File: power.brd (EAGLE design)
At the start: 65 x 80 mm, 21 parts, among them J1 Battery, J2 Solar, J3 Valve, J4 Button

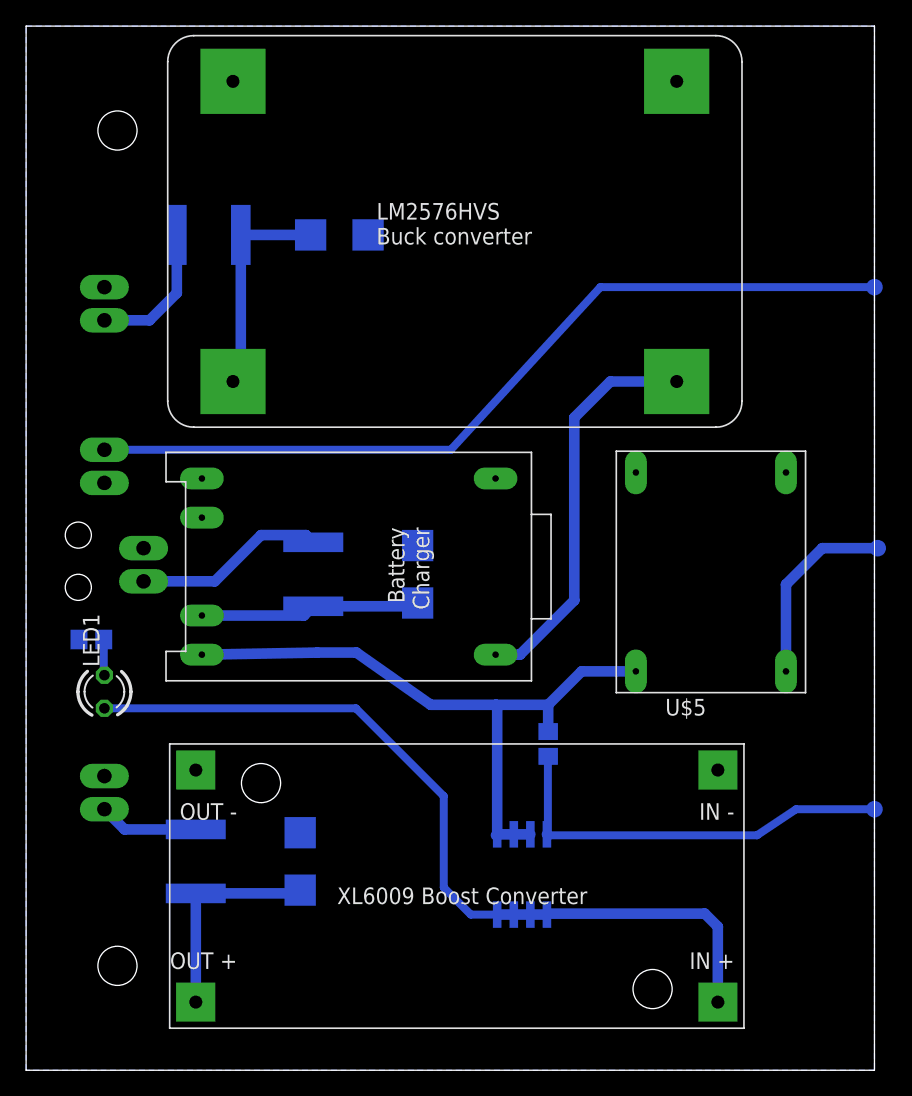
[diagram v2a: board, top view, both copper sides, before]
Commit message: Replaced PTC
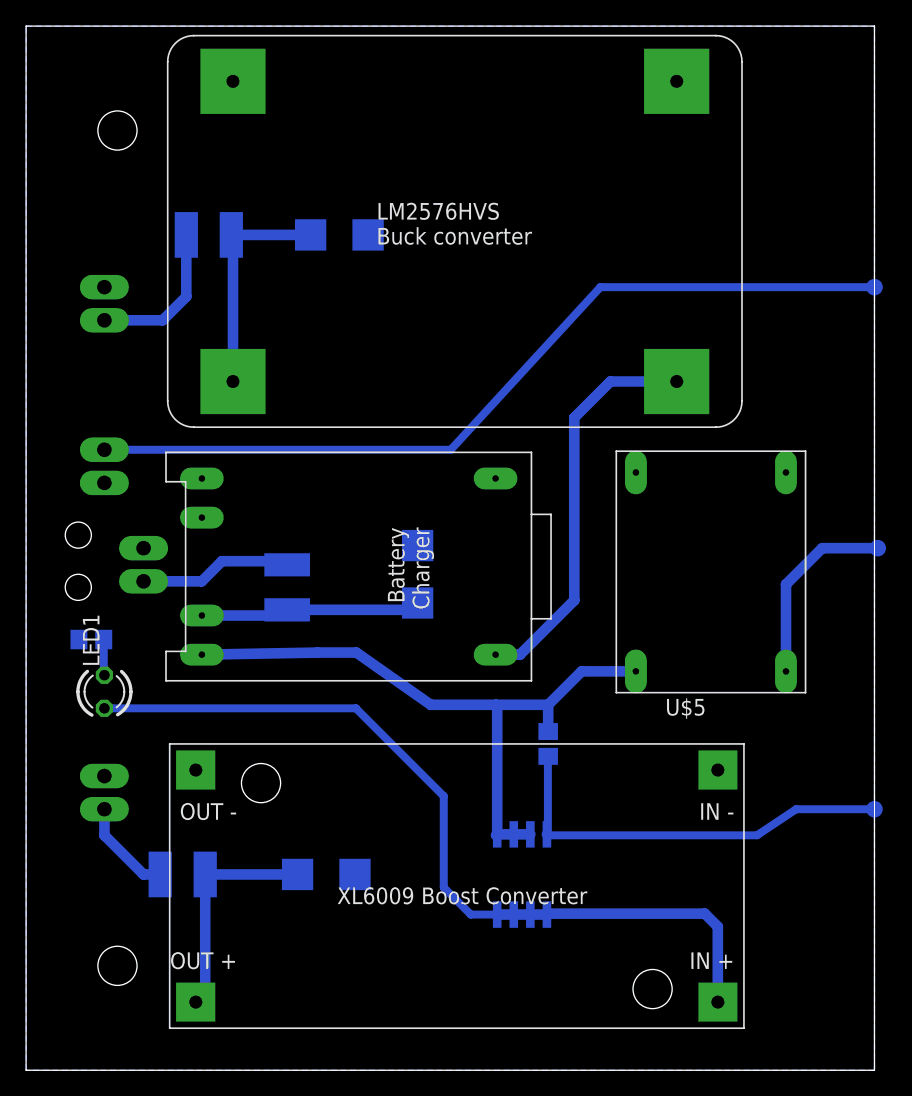
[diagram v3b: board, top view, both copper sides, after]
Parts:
- removed U$10: 500mA, fuse:MF-SMDF050
- removed U$11: 2A, fuse:MF-SMDF050
- added U$1: 1A, Semiconductors:1812
- added U$4: 2A, Semiconductors:1812
- D2, D3, D4: value (none) -> SJ24
- U$3: value 1A -> 2A; device fuse:MF-SMDF050 -> Semiconductors:1812
- moved D4 2.24 mm to (23.0, 15.0), turned to 180 degrees
- moved U$3 1.41 mm to (12.0, 15.0)
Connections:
- net N$3: now also U$4.P$1; no longer U$11.1
- net N$36: now also U$4.P$2; no longer U$11.2
- net N$6: now also U$3.P$1; no longer U$3.1
- net VALVE: now also U$3.P$2; no longer U$3.2
- net V_SOLAR: now also U$1.P$1; no longer U$10.1
- net V_SOLAR_FUSED: now also U$1.P$2; no longer U$10.2
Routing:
- net N$3: track 14.7 -> 11.8 mm
- net V_SOLAR: track 10.9 -> 11.8 mm
- net N$6: track 16.4 -> 17.2 mm
- net V_SOLAR_FUSED: track 16.8 -> 17.4 mm
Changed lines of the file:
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@@
 <layer number="230" name="230bmp" color="7" fill="1" visible="yes" active="yes"/>
 <layer number="231" name="231bmp" color="7" fill="1" visible="yes" active="yes"/>
+<layer number="232" name="Eagle3D_PG2" color="7" fill="1" visible="yes" active="yes"/>
+<layer number="233" name="Eagle3D_PG3" color="7" fill="1" visible="yes" active="yes"/>
 <layer number="248" name="Housing" color="7" fill="1" visible="yes" active="yes"/>
 <layer number="249" name="Edge" color="7" fill="1" visible="yes" active="yes"/>
@@
 </autorouter>
 <elements>
-<element name="D2" library="diode" library_urn="urn:adsk.eagle:library:210" package="SMB" package3d_urn="urn:adsk.eagle:package:43404/2" value="" x="24" y="64" rot="MR180"/>
-<element name="D3" library="diode" library_urn="urn:adsk.eagle:library:210" package="SMB" package3d_urn="urn:adsk.eagle:package:43404/2" value="" x="30" y="38" rot="MR90"/>
+<element name="D2" library="diode" library_urn="urn:adsk.eagle:library:210" package="SMB" package3d_urn="urn:adsk.eagle:package:43404/2" value="SJ24" x="24" y="64" rot="MR180"/>
+<element name="D3" library="diode" library_urn="urn:adsk.eagle:library:210" package="SMB" package3d_urn="urn:adsk.eagle:package:43404/2" value="SJ24" x="30" y="38" rot="MR90"/>
 <element name="J1" library="SparkFun-Connectors" package="1X02_LONGPADS" value="Battery" x="9" y="40" rot="R270"/>
 <element name="J2" library="SparkFun-Connectors" package="1X02_LONGPADS" value="Solar" x="6" y="60" rot="R270"/>
@@
 <attribute name="TP_SIGNAL_NAME" value="" x="65.25" y="40" size="1.778" layer="28" rot="MR0" display="off"/>
 </element>
-<element name="U$10" library="fuse" library_urn="urn:adsk.eagle:library:233" package="MF-SMDF050" package3d_urn="urn:adsk.eagle:package:14081/1" value="500mA" x="14" y="64" rot="MR180"/>
-<element name="U$11" library="fuse" library_urn="urn:adsk.eagle:library:233" package="MF-SMDF050" package3d_urn="urn:adsk.eagle:package:14081/1" value="2A" x="22" y="38" rot="MR270"/>
 <element name="U$2" library="breakout-modules" package="BATTERY_CHARGER" value="BATTERY_CHARGER" x="24.72" y="38.59" rot="R270"/>
 <element name="U$5" library="breakout-modules" package="QSKJ_BOOST_MODULE" value="QSKJ_BOOST_MODULE" x="52.47" y="38.18"/>
@@
 <element name="U$6" library="breakout-modules" package="XL6009_BOOST_MODULE" value="XL6009_BOOST_MODULE" x="53" y="23" rot="R180"/>
 <element name="U$9" library="Semiconductors" package="SO08" value="FDS6675" x="38" y="15" rot="MR180"/>
-<element name="U$3" library="fuse" library_urn="urn:adsk.eagle:library:233" package="MF-SMDF050" package3d_urn="urn:adsk.eagle:package:14081/1" value="1A" x="13" y="16" rot="MR90"/>
-<element name="D4" library="diode" library_urn="urn:adsk.eagle:library:210" package="SMB" package3d_urn="urn:adsk.eagle:package:43404/2" value="" x="21" y="16" rot="MR90"/>
+<element name="D4" library="diode" library_urn="urn:adsk.eagle:library:210" package="SMB" package3d_urn="urn:adsk.eagle:package:43404/2" value="SJ24" x="23" y="15" rot="MR180"/>
 <element name="J3" library="SparkFun-Connectors" package="1X02_LONGPADS" value="Valve" x="6" y="20" rot="R90"/>
 <element name="TP5" library="testpad" library_urn="urn:adsk.eagle:library:385" package="B1,27" package3d_urn="urn:adsk.eagle:package:27944/1" value="TPSB1,27" x="65" y="20" rot="MR0">
@@
 <attribute name="TP_SIGNAL_NAME" value="" x="65" y="60" size="1.778" layer="28" rot="MR90" display="off"/>
 </element>
+<element name="U$1" library="Semiconductors" package="1812" value="1A" x="14" y="64" rot="MR270"/>
+<element name="U$4" library="Semiconductors" package="1812" value="2A" x="20" y="37" rot="MR0"/>
+<element name="U$3" library="Semiconductors" package="1812" value="2A" x="12" y="15" rot="MR90"/>
 </elements>
 <signals>
@@
 <signal name="V_SOLAR_FUSED">
 <contactref element="U$8" pad="IN"/>
-<contactref element="U$10" pad="2"/>
 <contactref element="D2" pad="C"/>
-<wire x1="16.45" y1="64" x2="16.45" y2="53.37" width="0.8128" layer="16"/>
-<wire x1="16.45" y1="53.37" x2="15.85" y2="52.77" width="0.8128" layer="16"/>
-<wire x1="16.45" y1="64" x2="21.8" y2="64" width="0.8128" layer="16"/>
+<contactref element="U$1" pad="P$2"/>
+<wire x1="15.85" y1="52.77" x2="15.85" y2="63.875" width="0.8128" layer="16"/>
+<wire x1="15.85" y1="63.875" x2="15.725" y2="64" width="0.8128" layer="16"/>
+<wire x1="15.725" y1="64" x2="21.8" y2="64" width="0.8128" layer="16"/>
 </signal>
 <signal name="V_UNREG">
@@
 <signal name="V_SOLAR">
 <contactref element="J2" pad="2"/>
-<contactref element="U$10" pad="1"/>
-<wire x1="6" y1="57.46" x2="9.46" y2="57.46" width="0.8128" layer="16"/>
-<wire x1="11.55" y1="59.55" x2="11.55" y2="64" width="0.8128" layer="16"/>
-<wire x1="9.46" y1="57.46" x2="11.55" y2="59.55" width="0.8128" layer="16"/>
+<contactref element="U$1" pad="P$1"/>
+<wire x1="6" y1="57.46" x2="10.46" y2="57.46" width="0.8128" layer="16"/>
+<wire x1="12.275" y1="59.275" x2="12.275" y2="64" width="0.8128" layer="16"/>
+<wire x1="10.46" y1="57.46" x2="12.275" y2="59.275" width="0.8128" layer="16"/>
 </signal>
 <signal name="N$36">
 <contactref element="U$2" pad="V_BATT+"/>
-<contactref element="U$11" pad="2"/>
 <contactref element="D3" pad="C"/>
-<wire x1="13.47" y1="34.84" x2="21.29" y2="34.84" width="0.8128" layer="16"/>
-<wire x1="21.29" y1="34.84" x2="22" y2="35.55" width="0.8128" layer="16"/>
-<wire x1="22" y1="35.55" x2="29.75" y2="35.55" width="0.8128" layer="16"/>
-<wire x1="29.75" y1="35.55" x2="30" y2="35.8" width="0.8128" layer="16"/>
+<contactref element="U$4" pad="P$2"/>
+<wire x1="13.47" y1="34.84" x2="19.565" y2="34.84" width="0.8128" layer="16"/>
+<wire x1="19.565" y1="34.84" x2="20" y2="35.275" width="0.8128" layer="16"/>
+<wire x1="20" y1="35.275" x2="29.475" y2="35.275" width="0.8128" layer="16"/>
+<wire x1="29.475" y1="35.275" x2="30" y2="35.8" width="0.8128" layer="16"/>
 </signal>
 <signal name="N$3">
-<contactref element="U$11" pad="1"/>
 <contactref element="J1" pad="2"/>
-<wire x1="9" y1="37.46" x2="14.46" y2="37.46" width="0.8128" layer="16"/>
-<wire x1="14.46" y1="37.46" x2="18" y2="41" width="0.8128" layer="16"/>
-<wire x1="18" y1="41" x2="21.45" y2="41" width="0.8128" layer="16"/>
-<wire x1="21.45" y1="41" x2="22" y2="40.45" width="0.8128" layer="16"/>
+<contactref element="U$4" pad="P$1"/>
+<wire x1="9" y1="37.46" x2="13.46" y2="37.46" width="0.8128" layer="16"/>
+<wire x1="13.46" y1="37.46" x2="15" y2="39" width="0.8128" layer="16"/>
+<wire x1="15" y1="39" x2="19.725" y2="39" width="0.8128" layer="16"/>
+<wire x1="19.725" y1="39" x2="20" y2="38.725" width="0.8128" layer="16"/>
 </signal>
 <signal name="N$9">
@@
 </signal>
 <signal name="VALVE">
-<contactref element="U$3" pad="2"/>
 <contactref element="J3" pad="1"/>
-<wire x1="6" y1="20" x2="7.55" y2="18.45" width="0.8128" layer="16"/>
-<wire x1="7.55" y1="18.45" x2="13" y2="18.45" width="0.8128" layer="16"/>
+<contactref element="U$3" pad="P$2"/>
+<wire x1="10.275" y1="15" x2="9" y2="15" width="0.8128" layer="16"/>
+<wire x1="9" y1="15" x2="6" y2="18" width="0.8128" layer="16"/>
+<wire x1="6" y1="18" x2="6" y2="20" width="0.8128" layer="16"/>
 </signal>
 <signal name="N$6">
 <contactref element="U$6" pad="V_OUT"/>
-<contactref element="U$3" pad="1"/>
 <contactref element="D4" pad="C"/>
-<wire x1="13" y1="5.22" x2="13" y2="13.55" width="0.8128" layer="16"/>
-<wire x1="13" y1="13.55" x2="20.75" y2="13.55" width="0.8128" layer="16"/>
-<wire x1="20.75" y1="13.55" x2="21" y2="13.8" width="0.8128" layer="16"/>
+<contactref element="U$3" pad="P$1"/>
+<wire x1="13" y1="5.22" x2="13.725" y2="5.945" width="0.8128" layer="16"/>
+<wire x1="13.725" y1="5.945" x2="13.725" y2="15" width="0.8128" layer="16"/>
+<wire x1="13.725" y1="15" x2="20.8" y2="15" width="0.8128" layer="16"/>
 </signal>
 <signal name="BUTTON_WAKEUP_INT">

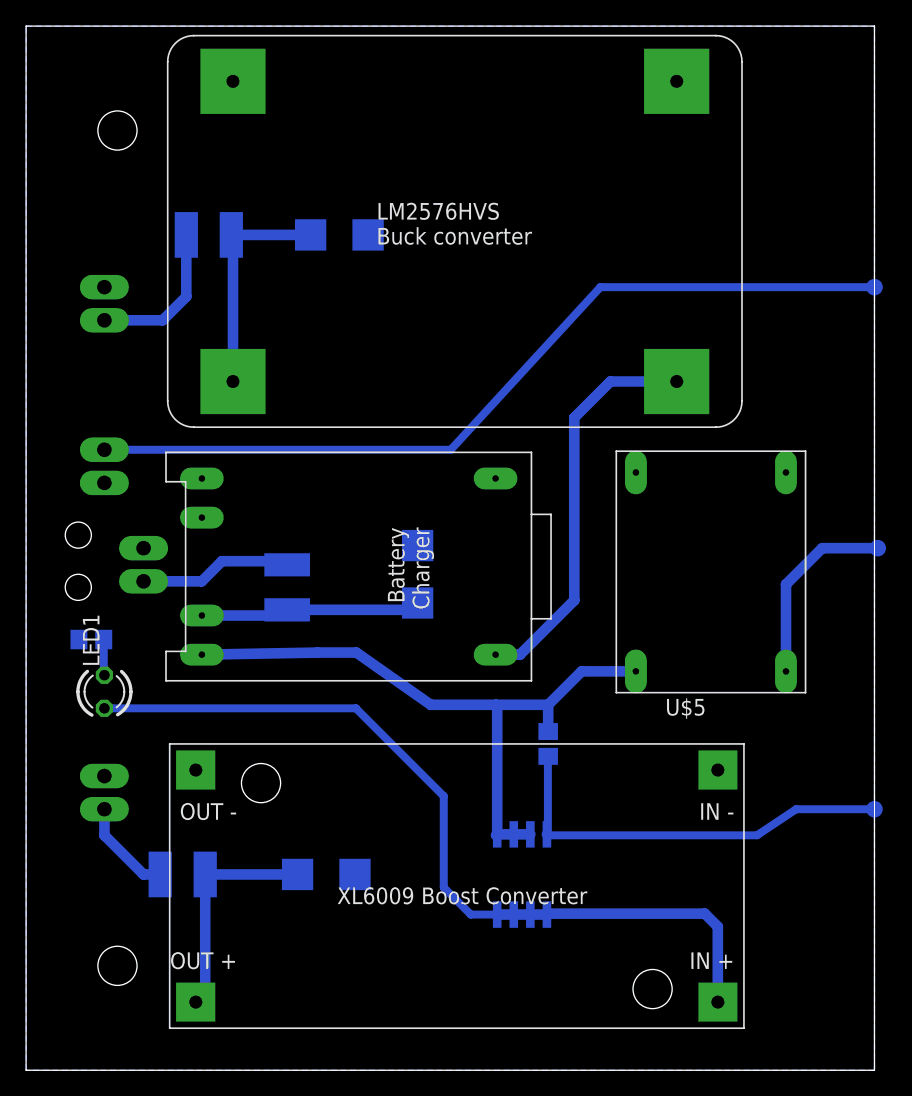
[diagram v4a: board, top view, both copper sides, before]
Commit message: Using CN3791
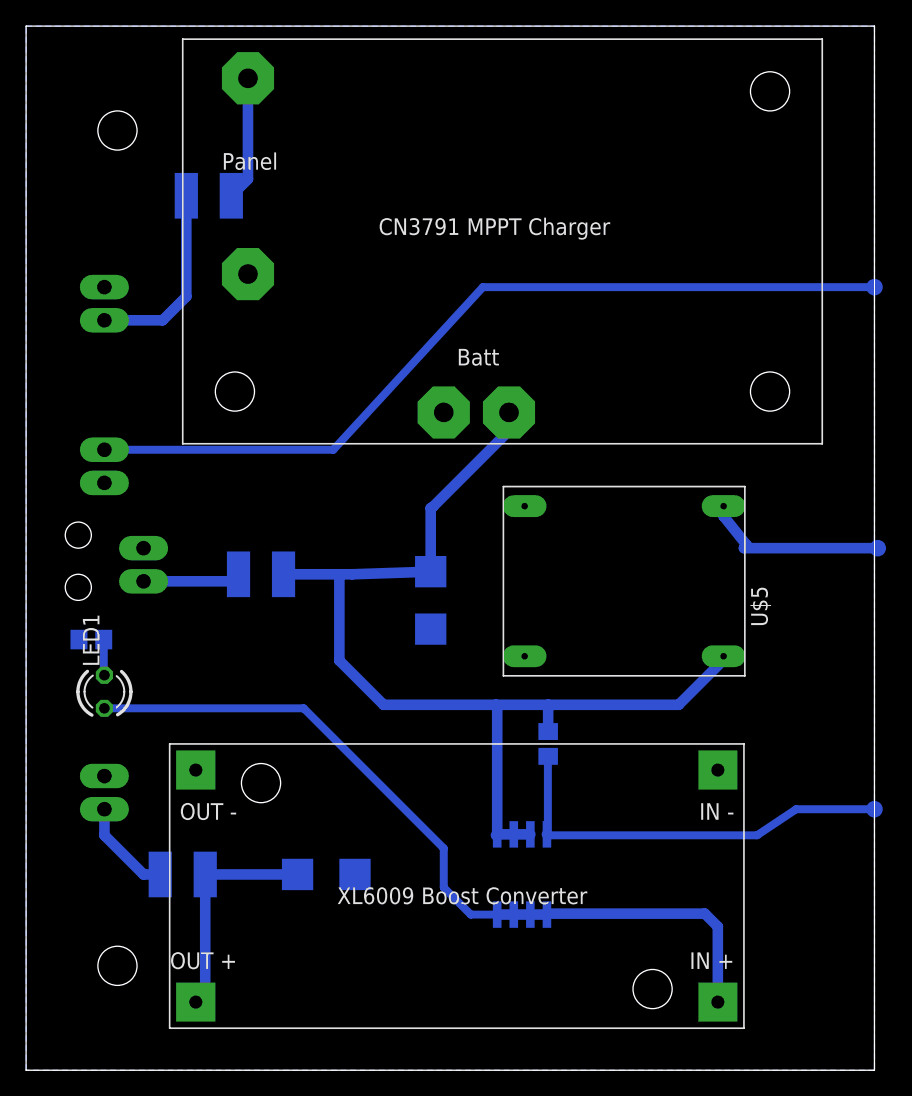
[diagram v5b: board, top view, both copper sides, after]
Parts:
- removed D2: SJ24, diode:SMB
- removed U$8: LM2576HVS_BUCK_MODULE, breakout-modules:LM2576HVS_BUCK_MODULE
- U$2: value BATTERY_CHARGER -> CN3791_MTTP_LIPO_SOLAR_CHARGER; device breakout-modules:BATTERY_CHARGER -> breakout-modules:CN3791_MPPT_LIPO_SOLAR_CHARGER
- moved U$2 15.8 mm to (12.0, 48.0), turned to 0 degrees
- moved U$5 6.69 mm to (45.8, 37.5), turned to 90 degrees
- moved U$1 3.00 mm to (14.0, 67.0)
- moved D3 2.24 mm to (31.0, 36.0), turned to 270 degrees
- moved U$4 2.24 mm to (18.0, 38.0), turned to 270 degrees
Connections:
- removed net N$36: D3.C, U$2.V_BATT+, U$4.P$2
- removed net V_CHARGER: U$2.V_IN, U$8.OUT
- net GND: no longer D2.A, U$2.V_BATT-, U$8.GND@1, U$8.GND@2
- net V_SOLAR_FUSED: now also U$2.PANEL; no longer D2.C, U$8.IN
- net V_UNREG: now also D3.C, U$2.BATT+, U$4.P$2; no longer U$2.V_OUT
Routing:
- net V_CHARGER: track 30.8 -> 0.00 mm
- net V_UNREG: track 50.3 -> 79.8 mm
- net N$36: track 16.9 -> 0.00 mm
- net V_SOLAR_FUSED: track 17.4 -> 9.70 mm
- net N$3: track 11.8 -> 7.50 mm
- net V_SOLAR: track 11.8 -> 14.8 mm
- net V_VALVE_UNREG: track 63.9 -> 61.5 mm
- net VCC5: track 14.8 -> 14.2 mm
